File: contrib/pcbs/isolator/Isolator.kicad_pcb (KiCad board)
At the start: 2 copper layers, 30.5 x 17.8 mm, 11 parts, among them J1 USB-to-UART, J2 Power, J3 UART-to-Device, J4 Power, U1 FOD8012

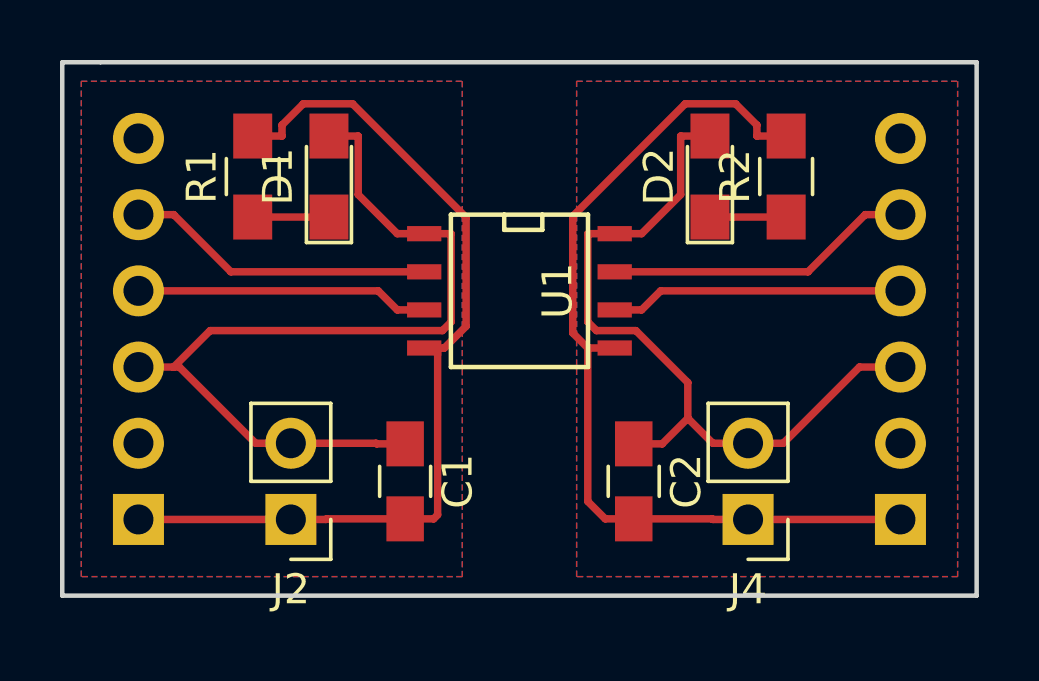
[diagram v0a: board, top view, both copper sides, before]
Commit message: Rework contributed PCBs
* Upgrade to KiCad 8
* Improved PCBs
* Added Makefile for automation of schema and board renders
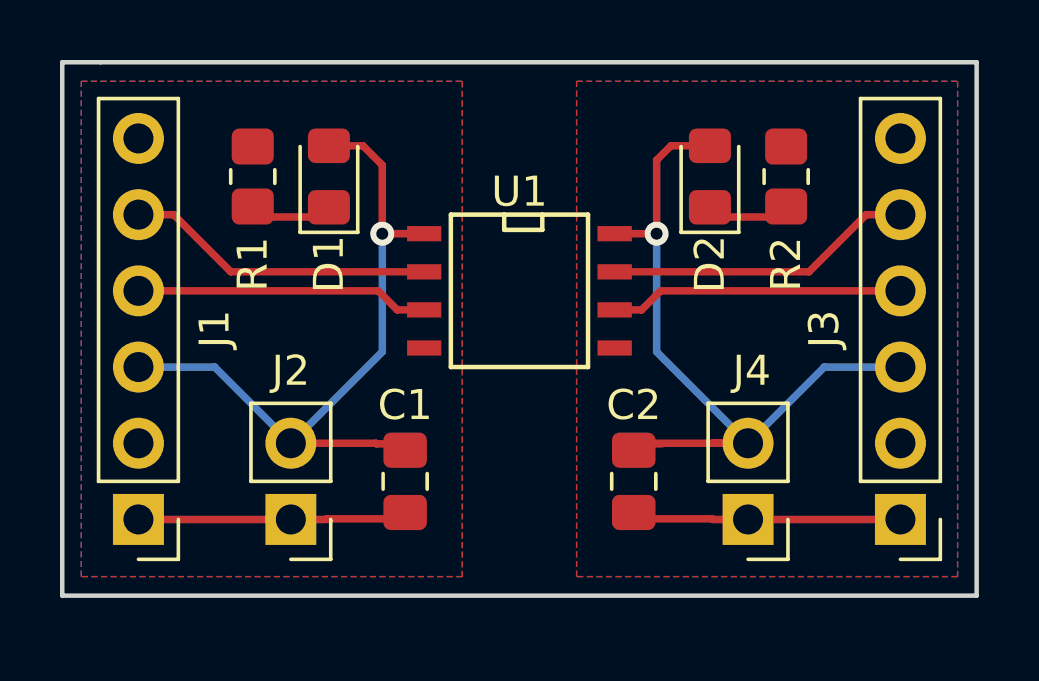
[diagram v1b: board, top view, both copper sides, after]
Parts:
- C1, C2: footprint Capacitors_SMD:C_0805_HandSoldering -> Capacitor_SMD:C_0805_2012Metric_Pad1.18x1.45mm_HandSolder
- D1, D2: footprint LEDs:LED_0805_HandSoldering -> LED_SMD:LED_0805_2012Metric_Pad1.15x1.40mm_HandSolder
- J1: footprint Socket_Strips:Socket_Strip_Angled_1x06_Pitch2.54mm -> Connector_PinHeader_2.54mm:PinHeader_1x06_P2.54mm_Vertical; moved to F.Cu
- J2, J4: footprint Socket_Strips:Socket_Strip_Straight_1x02_Pitch2.54mm -> Connector_PinHeader_2.54mm:PinHeader_1x02_P2.54mm_Vertical
- J3: footprint Pin_Headers:Pin_Header_Angled_1x06_Pitch2.54mm -> Connector_PinHeader_2.54mm:PinHeader_1x06_P2.54mm_Vertical; moved to F.Cu
- R1, R2: footprint Resistors_SMD:R_0805_HandSoldering -> Resistor_SMD:R_0805_2012Metric_Pad1.20x1.40mm_HandSolder
- turned J1 to 180 degrees
- turned J3 to 180 degrees
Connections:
- J1 pad 2: (no net) -> unconnected-(J1-Pin_2-Pad2)
- J1 pad 6: (no net) -> unconnected-(J1-Pin_6-Pad6)
- J3 pad 2: (no net) -> unconnected-(J3-Pin_2-Pad2)
- J3 pad 6: (no net) -> unconnected-(J3-Pin_6-Pad6)
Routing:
- net GNDA: track 30.6 -> 9.03 mm
- net GND: track 30.3 -> 8.90 mm
- net VDD: track 29.3 -> 23.9 mm, vias 0 -> 1
- net VDDA: track 25.5 -> 26.2 mm, vias 0 -> 1
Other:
- net class Default removed
